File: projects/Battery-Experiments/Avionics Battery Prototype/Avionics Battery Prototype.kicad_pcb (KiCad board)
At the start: 2 copper layers, 134 x 139.7 mm, 60 parts, among them J1 Jack-DC, J2 Enable, J3 UART, J4 SBW JTAG, U1 OPA4197, U2 OPA4197, U3 CD4052B, U4 LT1763, U5 MSP430G2233, U6 CD40109B

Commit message: AVB Rev C Final
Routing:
- net GND: track 77.3 -> 88.0 mm, vias 3 -> 5
- net Net-(J1-Pad1): track 79.5 -> 71.0 mm

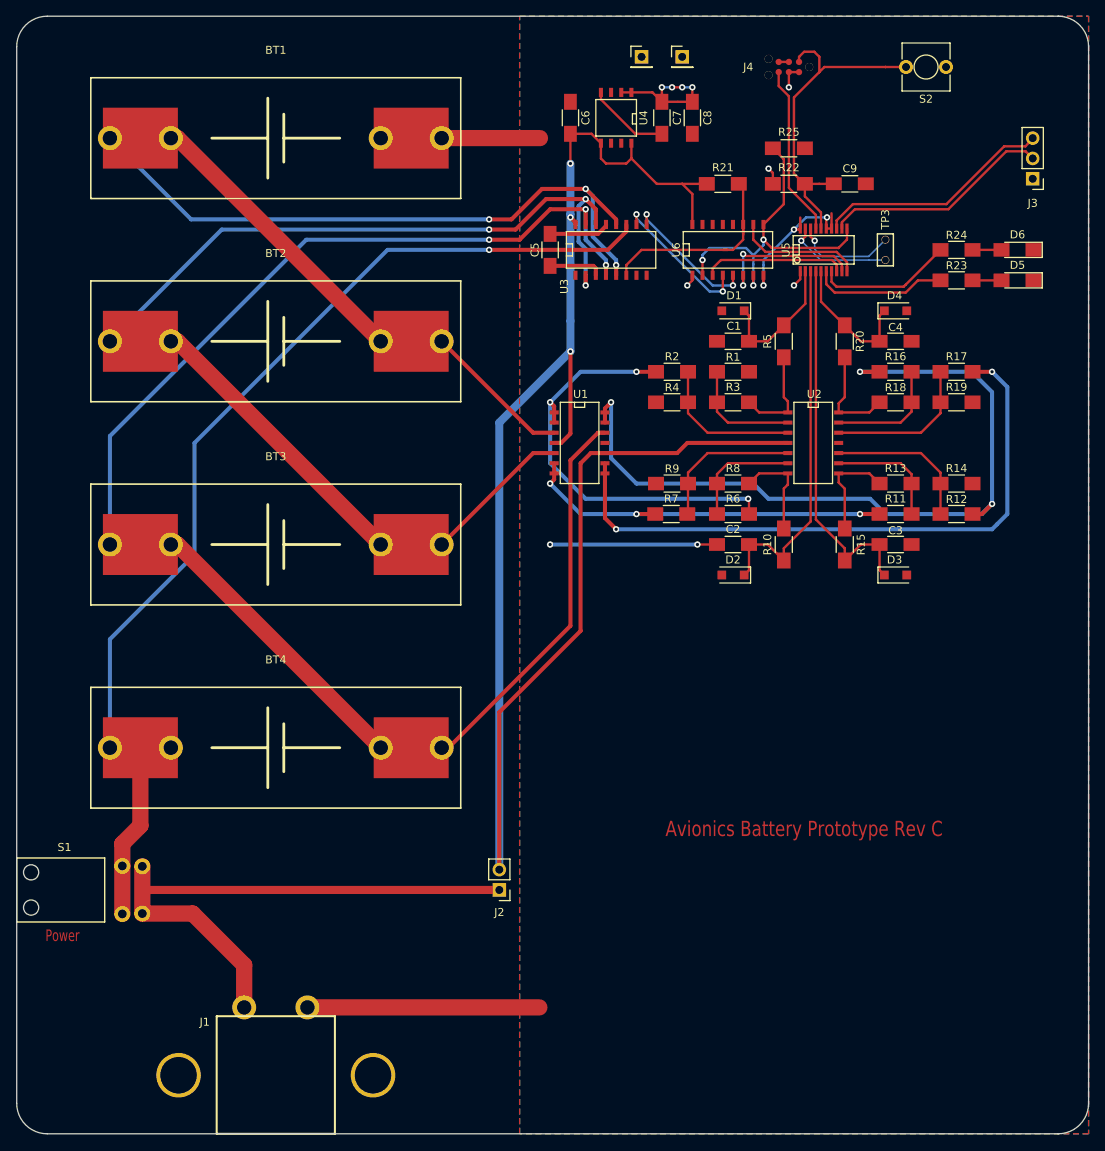
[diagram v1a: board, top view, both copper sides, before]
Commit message: AVB Rev C and XTAL Plug Final
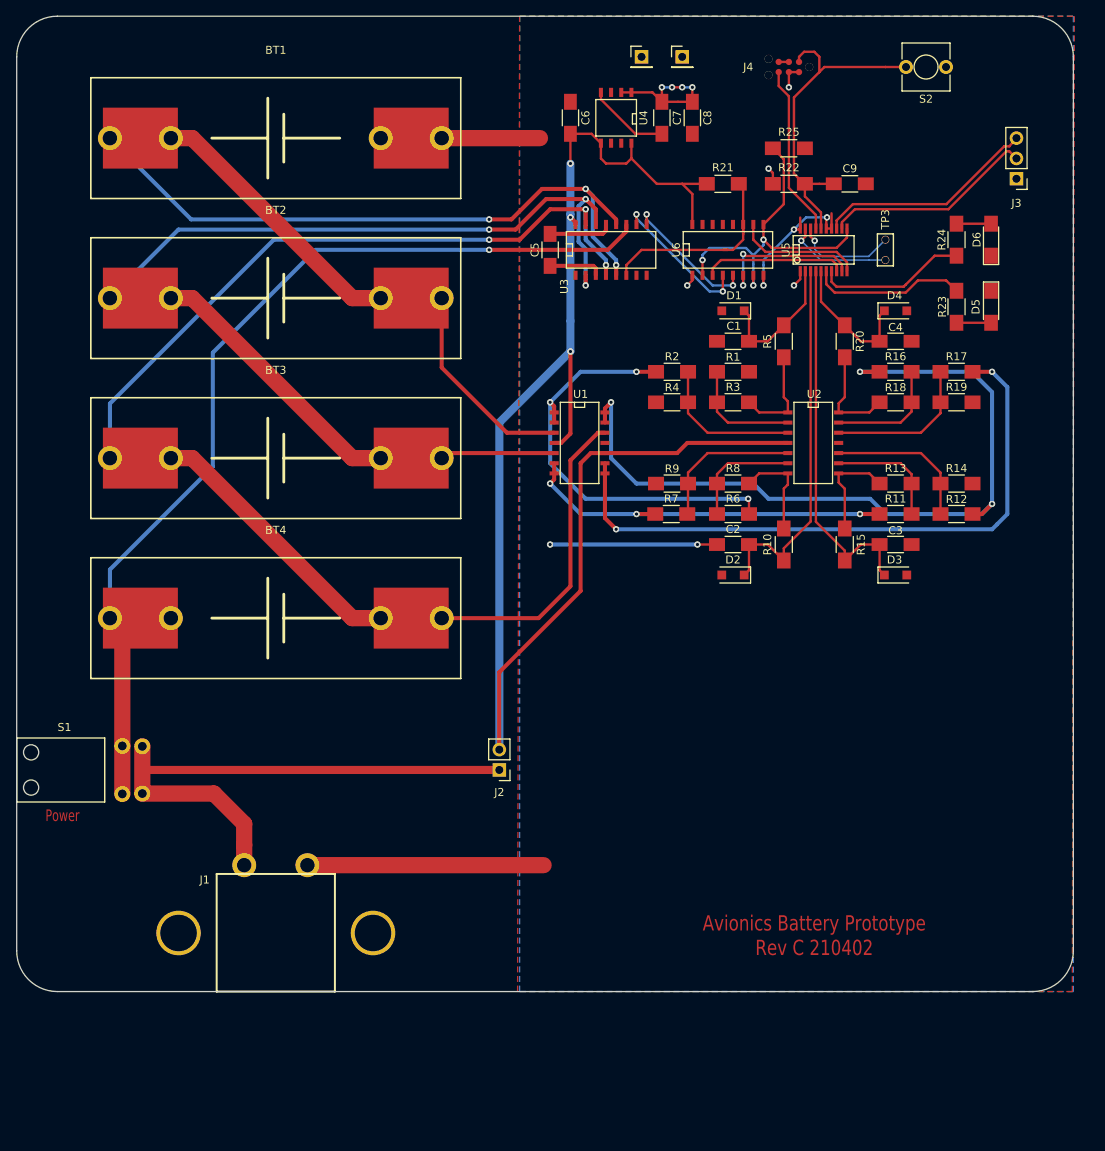
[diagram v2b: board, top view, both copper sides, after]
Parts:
- moved J1 17.8 mm to (71.1, 149.9)
- moved BT4 16.2 mm to (71.1, 103.2)
- moved J2 15.0 mm to (99.1, 122.2)
- moved S1 15.0 mm to (38.7, 122.2)
- moved G*** 13.4 mm to (138.4, 132.7)
- moved BT3 10.8 mm to (71.1, 83.2)
- moved BT2 5.40 mm to (71.1, 63.2)
- moved D5 4.67 mm to (160.5, 64.3), turned to 270 degrees
- moved D6 3.54 mm to (160.5, 55.9), turned to 90 degrees
- moved R23 3.30 mm to (156.2, 64.3), turned to 270 degrees
- moved J3 2.03 mm to (163.7, 48.3)
- moved R24 1.27 mm to (156.2, 55.9), turned to 90 degrees
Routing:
- net +BATT: track 220.4 -> 190.4 mm
- net Net-(BT3-Pad1): track 189.2 -> 172.7 mm
- net Net-(BT1-Pad1): track 143.0 -> 153.5 mm
- net Net-(BT4-Pad1): track 130.0 -> 120.3 mm
- net Net-(BT2-Pad1): track 142.9 -> 137.7 mm
- net Net-(R23-Pad1): track 17.0 -> 19.5 mm
- net UART_TX: track 29.8 -> 27.8 mm
- net UART_RX: track 28.7 -> 26.6 mm
- net Net-(R24-Pad1): track 17.1 -> 18.8 mm
- net Net-(J1-Pad1): track 71.0 -> 69.8 mm
- net Net-(D6-Pad2): track 3.62 -> 4.32 mm
- net Net-(D5-Pad2): track 3.62 -> 4.32 mm
- net GND: track 88.0 -> 88.6 mm
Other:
- board size 134 x 139.7 mm -> 132.1 x 121.9 mm
- board text added: "Avionics Battery Prototype Rev C 210402"
- board text removed: "Avionics Battery Prototype Rev C"
